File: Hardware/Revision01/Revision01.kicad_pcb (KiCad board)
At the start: 4 copper layers, 100 x 119.8 mm, 84 parts, among them J1 Battery connector, J2 StrainConn, J3 StrainConn, J4 StrainConn, J5 StrainConn, J6 StrainConn, J7 StrainConn, J8 StrainConn, J9 StrainConn, Q1 PMOS, Q2 NMOS, Q3 PMOS, SW1 SW_SPST_LED, U1 NCP1117LPST50T3G, U2 NUCLEO-L476RG, U4 LP5813BDRRR, U5 MRF89XAM9AT-I/RM, U6 ICM-45605

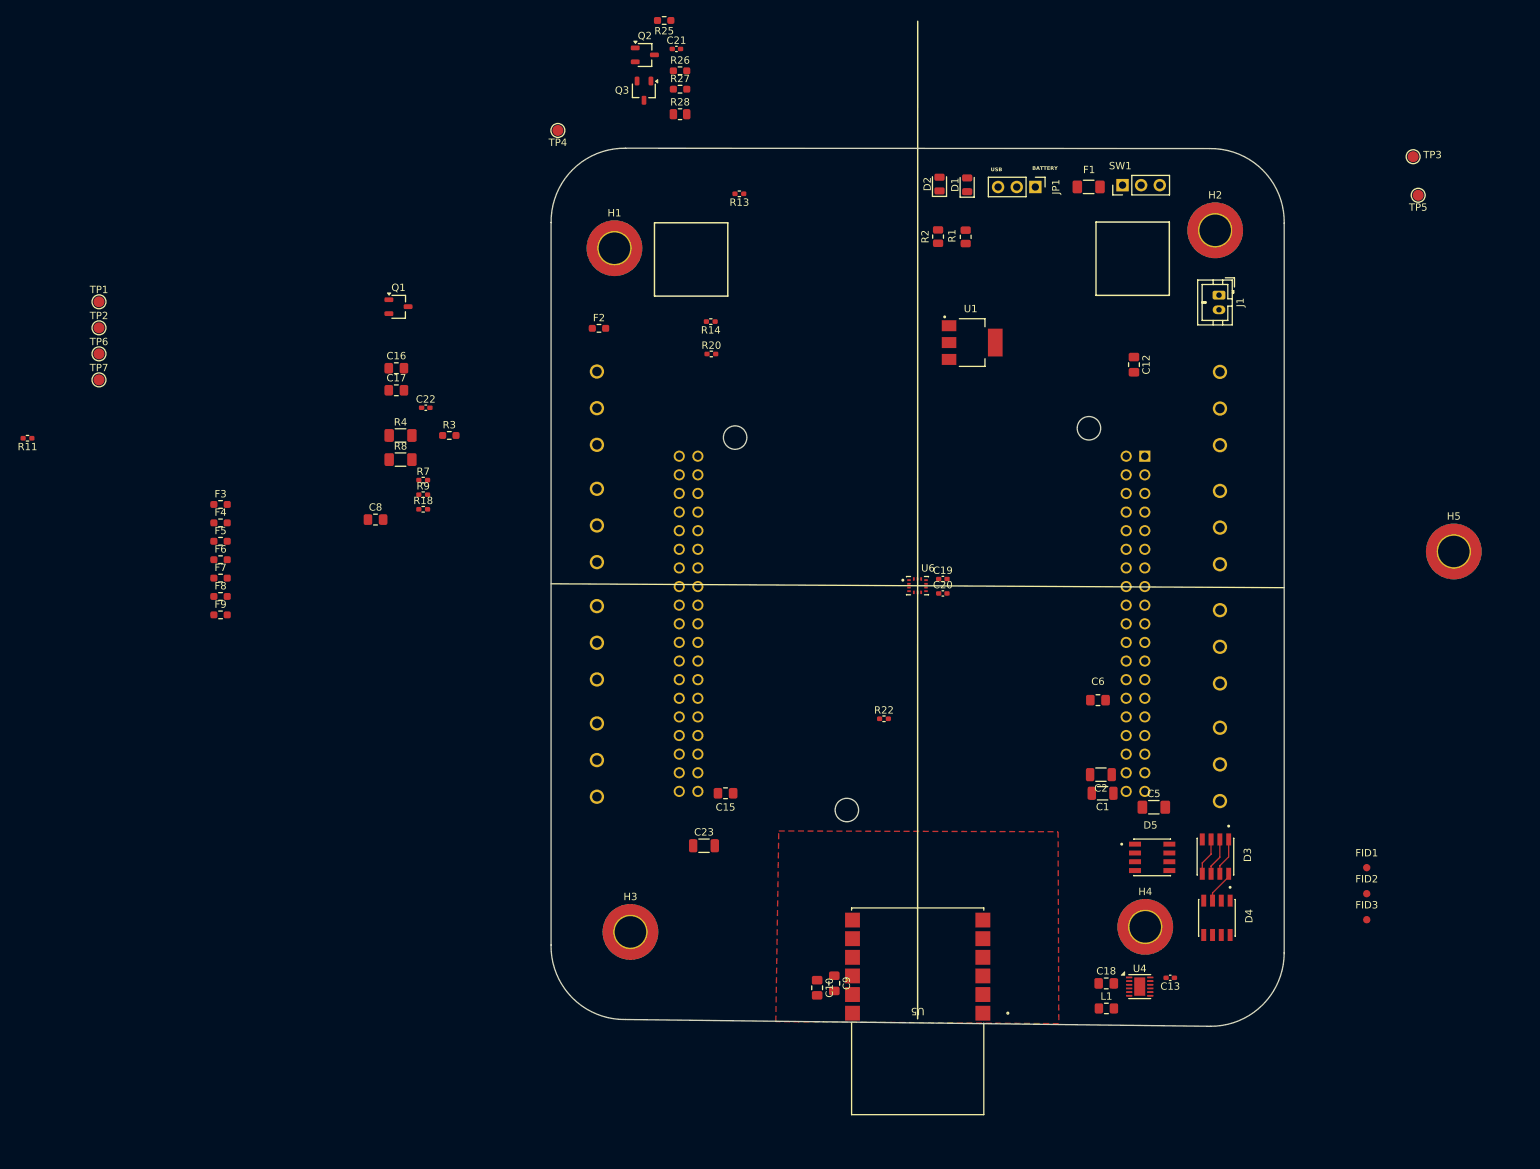
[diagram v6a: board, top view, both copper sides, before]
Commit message: Started working on PART B schematic, making small changes on PART A
ADC uncertainty calculated to be 1.22%
Added External GPIO's that may or may not use
	 start/stop, indication RGB leds

Started working on PART B schematic on ALTIUM, properly imported components with footprints
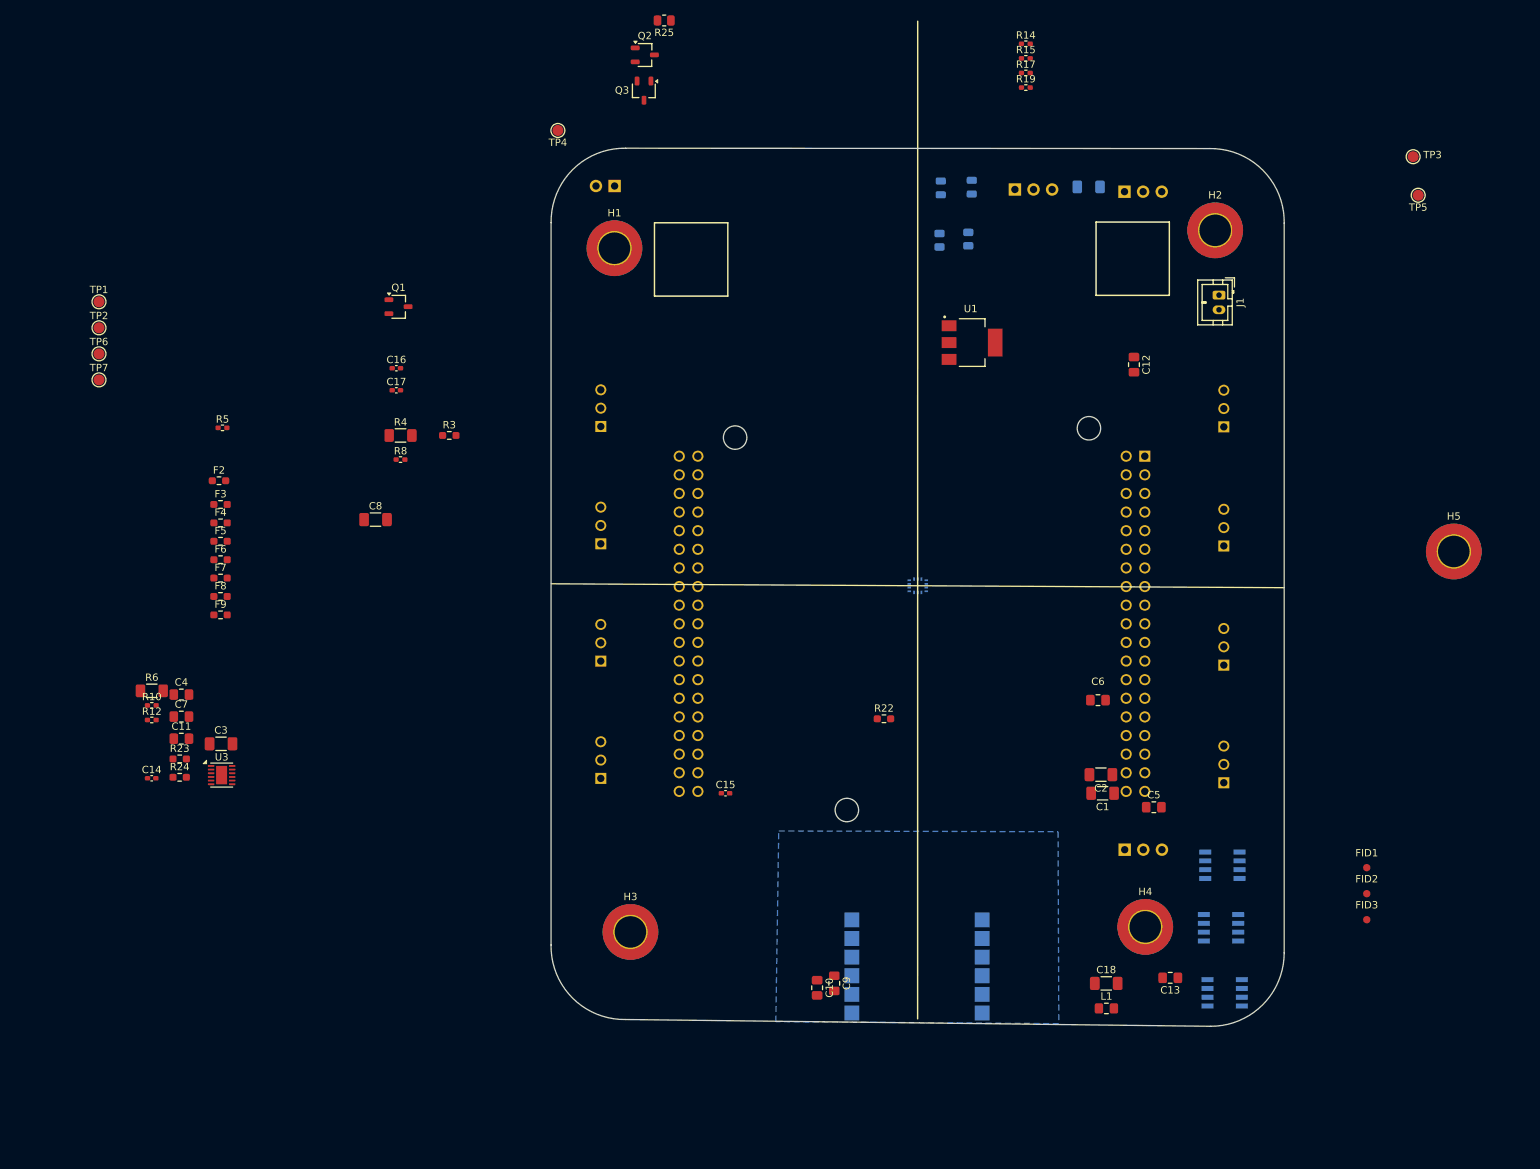
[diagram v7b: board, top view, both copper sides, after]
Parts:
- removed C19, C20, C21, C22: 0.1uF, Capacitor_SMD:C_0402_1005Metric_Pad0.74x0.62mm_HandSolder
- removed C23: 10uF, Capacitor_SMD:C_1206_3216Metric
- removed R11, R13, R18, R20, R7, R9: 1.6K +-1%, Resistor_SMD:R_0402_1005Metric_Pad0.72x0.64mm_HandSolder
- removed R26: 10K +-1%, Resistor_SMD:R_0603_1608Metric_Pad0.98x0.95mm_HandSolder
- removed R27: 15K +-1%, Resistor_SMD:R_0603_1608Metric_Pad0.98x0.95mm_HandSolder
- removed R28: 3.3K +-1%, Resistor_SMD:R_0805_2012Metric
- removed U6: ICM-45605, ICM-45605-gyroscope:XDCR_ICM-45605
- added C11: 10nF, Capacitor_SMD:C_0805_2012Metric_Pad1.18x1.45mm_HandSolder, F.Cu at (60.6, 113.5)
- added C14: 0.1uF, Capacitor_SMD:C_0402_1005Metric_Pad0.74x0.62mm_HandSolder, F.Cu at (56.5, 118.9)
- added C3: 100uF, Capacitor_SMD:C_1206_3216Metric_Pad1.33x1.80mm_HandSolder, F.Cu at (66.0, 114.2)
- added C4: 10nF, Capacitor_SMD:C_0805_2012Metric_Pad1.18x1.45mm_HandSolder, F.Cu at (60.6, 107.5)
- added C7: 10nF, Capacitor_SMD:C_0805_2012Metric_Pad1.18x1.45mm_HandSolder, F.Cu at (60.6, 110.5)
- added D6: RGBW_LED, RGBW:SOL120P540X160-8N, B.Cu at (202.9, 148.2)
- added R10: 1.6K +-1%, Resistor_SMD:R_0402_1005Metric_Pad0.72x0.64mm_HandSolder, F.Cu at (56.6, 109.0)
- added R12: 1.6K +-1%, Resistor_SMD:R_0402_1005Metric_Pad0.72x0.64mm_HandSolder, F.Cu at (56.6, 110.9)
- added R15: 1.6K +-1%, Resistor_SMD:R_0402_1005Metric_Pad0.72x0.64mm_HandSolder, F.Cu at (175.8, 20.7)
- added R17: 1.6K +-1%, Resistor_SMD:R_0402_1005Metric_Pad0.72x0.64mm_HandSolder, F.Cu at (175.8, 22.7)
- added R19: 1.6K +-1%, Resistor_SMD:R_0402_1005Metric_Pad0.72x0.64mm_HandSolder, F.Cu at (175.8, 24.7)
- added R23: 10K +-1%, Resistor_SMD:R_0603_1608Metric_Pad0.98x0.95mm_HandSolder, F.Cu at (60.4, 116.2)
- added R24: 15K +-1%, Resistor_SMD:R_0603_1608Metric_Pad0.98x0.95mm_HandSolder, F.Cu at (60.4, 118.8)
- added R5: 1.6K +-1%, Resistor_SMD:R_0402_1005Metric_Pad0.72x0.64mm_HandSolder, F.Cu at (66.2, 71.1)
- added R6: 0K +-1%, Resistor_SMD:R_1206_3216Metric_Pad1.30x1.75mm_HandSolder, F.Cu at (56.6, 107.0)
- added SW2: ON/OFF_SW_SPST_LED, Connector_PinHeader_2.54mm:PinHeader_1x03_P2.54mm_Vertical, B.Cu at (189.2, 38.9)
- added U3: LP5813BDRRR, Package_SON:WSON-12-1EP_3x3mm_P0.5mm_EP1.5x2.5mm, F.Cu at (66.1, 118.5)
- C1, C2: footprint Capacitor_SMD:C_1206_3216Metric -> Capacitor_SMD:C_1206_3216Metric_Pad1.33x1.80mm_HandSolder
- C13: value 10uF -> 22uF; footprint Capacitor_SMD:C_0402_1005Metric_Pad0.74x0.62mm_HandSolder -> Capacitor_SMD:C_0805_2012Metric_Pad1.18x1.45mm_HandSolder
- C15, C16, C17: value 10nF -> 0.1uF; footprint Capacitor_SMD:C_0805_2012Metric_Pad1.18x1.45mm_HandSolder -> Capacitor_SMD:C_0402_1005Metric_Pad0.74x0.62mm_HandSolder
- C18: value 22uF -> 10uF; footprint Capacitor_SMD:C_0805_2012Metric_Pad1.18x1.45mm_HandSolder -> Capacitor_SMD:C_1206_3216Metric_Pad1.33x1.80mm_HandSolder
- C5: value 100uF -> 10nF; footprint Capacitor_SMD:C_1206_3216Metric_Pad1.33x1.80mm_HandSolder -> Capacitor_SMD:C_0805_2012Metric_Pad1.18x1.45mm_HandSolder
- C8: value 10nF -> 10uF; footprint Capacitor_SMD:C_0805_2012Metric_Pad1.18x1.45mm_HandSolder -> Capacitor_SMD:C_1206_3216Metric_Pad1.33x1.80mm_HandSolder
- D1, D2, D4, D5, F1, JP1, R1, R2: moved to B.Cu
- D3: value RGBW_LED -> Indicication_RGB_Led; footprint RGBW:SOL120P540X160-8N -> Connector_PinHeader_2.54mm:PinHeader_1x03_P2.54mm_Vertical; moved to B.Cu
- J2, J3, J4, J5, J6, J7, J8, J9: footprint 691137710003:691137710003 -> JST:JST_B3B-XH-A
- R22: value 1.6K +-1% -> 10K +-1%; footprint Resistor_SMD:R_0402_1005Metric_Pad0.72x0.64mm_HandSolder -> Resistor_SMD:R_0603_1608Metric_Pad0.98x0.95mm_HandSolder
- R25: value 10K +-1% -> 3.3K +-1%; footprint Resistor_SMD:R_0603_1608Metric_Pad0.98x0.95mm_HandSolder -> Resistor_SMD:R_0805_2012Metric
- R8: value 0K +-1% -> 1.6K +-1%; footprint Resistor_SMD:R_1206_3216Metric_Pad1.30x1.75mm_HandSolder -> Resistor_SMD:R_0402_1005Metric_Pad0.72x0.64mm_HandSolder
- SW1: value SW_SPST_LED -> StartStop_Push; footprint Connector_PinHeader_2.54mm:PinHeader_1x03_P2.54mm_Vertical -> Connector_PinHeader_2.54mm:PinHeader_1x02_P2.54mm_Vertical; moved to B.Cu
- U4: value LP5813BDRRR -> MRF89XAM9AT-I/RM; footprint Package_SON:WSON-12-1EP_3x3mm_P0.5mm_EP1.5x2.5mm -> MRF89XAM9AT-antenna:MOD_MRF89XAM9A_MCH; moved to B.Cu
- U5: value MRF89XAM9AT-I/RM -> ICM-45605; footprint MRF89XAM9AT-antenna:MOD_MRF89XAM9A_MCH -> ICM-45605-gyroscope:XDCR_ICM-45605; moved to B.Cu
- moved SW1 69.3 mm to (119.7, 38.1)
- moved U5 58.0 mm to (161.0, 92.6), turned to 0 degrees
- moved R14 57.3 mm to (175.8, 18.7), turned to 0 degrees
- moved F2 55.8 mm to (65.7, 78.3)
- moved U4 30.6 mm to (160.9, 150.7)
- moved D5 13.4 mm to (202.4, 139.3), turned to 180 degrees
- moved D3 12.4 mm to (189.3, 128.6)
- moved D4 7.21 mm to (202.6, 130.8), turned to 180 degrees
- moved D2 4.42 mm to (168.4, 38.3)
- moved R2 4.13 mm to (167.9, 45.3)
- moved D1 3.62 mm to (164.2, 38.4)
- moved R1 3.60 mm to (164.0, 45.5)
- moved JP1 2.81 mm to (174.3, 38.6)
- turned F1 to 180 degrees
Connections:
- C10 pad 1: /AIN_4 -> /AIN_6
- C12 pad 1: /AIN_5 -> /AIN_8
- C13 pad 1: +3.3V -> Net-(U3-VOUT)
- C15 pad 1: /AIN_6 -> +3.3V
- C16 pad 1: /AIN_7 -> /BatteryV_AIN
- C17 pad 1: /AIN_8 -> +3.3V
- C18 pad 1: Net-(U4-VOUT) -> +3.3V
- C5 pad 1: /Application/+StrainV -> /AIN_2
- C6 pad 1: /AIN_1 -> /AIN_3
- C8 pad 1: /AIN_2 -> +3.3V
- C9 pad 1: /AIN_3 -> /AIN_5
- D4 pad 1: /Application/U1_OUT2 -> /Application/U1_OUT1
- D4 pad 2: /Application/U1_OUT3 -> /Application/U1_OUT2
- D4 pad 3: /Application/U1_OUT0 -> /Application/U1_OUT3
- D4 pad 4: /Application/U1_OUT1 -> /Application/U1_OUT0
- D5 pad 1: /Application/U1_OUT3 -> /Application/U1_OUT2
- D5 pad 2: /Application/U1_OUT0 -> /Application/U1_OUT3
- D5 pad 3: /Application/U1_OUT1 -> /Application/U1_OUT0
- D5 pad 4: /Application/U1_OUT2 -> /Application/U1_OUT1
- F1 pad 2: Net-(SW1-K) -> Net-(SW2-K)
- L1 pad 2: Net-(U4-SW) -> Net-(U3-SW)
- R22 pad 1: /Application/OpAmpOutput8 -> Earth
- R22 pad 2: /AIN_8 -> /BatteryV_Div_Enable_GPIO
- R25 pad 2: /BatteryV_Div_Enable_GPIO -> /BatteryV_AIN
- R8 pad 1: Net-(Q1-S) -> /Application/OpAmpOutput2
- R8 pad 2: +3.3V -> /AIN_2
- SW1 pad 1: Net-(SW1-K) -> /STARTSTOP_GPIO
- SW1 pad 2: Net-(J1-Pin_2) -> Earth
- U2 pad CN10_21: unconnected-(U2B-PA9-PadCN10_21) -> /STARTSTOP_GPIO
- U4 pad 1: Net-(U4-SW) -> Earth
- U4 pad 10: /Application/U1_OUT0 -> +3.3V
- U4 pad 11: /LP5813_EN_GPIO -> Earth
- U4 pad 12: +3.3V -> Earth
- U4 pad 2: Net-(U4-VOUT) -> /ANT_RESET_ANT_GPIO
- U4 pad 3: Earth -> /ANT_CSCON_GPIO
- U4 pad 4: unconnected-(U4-SYNC-Pad4) -> /ANT_IRQ0_GPIO
- U4 pad 5: /I2C_SCL -> /PB15_SPI2_MOSI
- U4 pad 6: /I2C_SDA -> /PB13_SPI2_SCK
- U4 pad 7: /Application/U1_OUT3 -> /PB14_SPI2_MISO
- U4 pad 8: /Application/U1_OUT2 -> /ANT_CSDATA_GPIO
- U4 pad 9: /Application/U1_OUT1 -> /ANT_IRQ1_GPIO
- U5 pad 1: Earth -> /PB14_SPI2_MISO
- U5 pad 10: +3.3V -> unconnected-(U5-RESV_10-Pad10)
- U5 pad 11: Earth -> unconnected-(U5-RESV_11-Pad11)
- U5 pad 12: Earth -> /ICM_CS_GPIO
- U5 pad 2: /ANT_RESET_ANT_GPIO -> unconnected-(U5-RESV/MAS_DA-Pad2)
- U5 pad 3: /ANT_CSCON_GPIO -> unconnected-(U5-RESV/MAS_CLK-Pad3)
- U5 pad 4: /ANT_IRQ0_GPIO -> /ICM_INT1_GPIO
- U5 pad 5: /PB15_SPI2_MOSI -> +3.3V
- U5 pad 6: /PB13_SPI2_SCK -> Earth
- U5 pad 7: /PB14_SPI2_MISO -> unconnected-(U5-RESV_7-Pad7)
- U5 pad 8: /ANT_CSDATA_GPIO -> +3.3V
- U5 pad 9: /ANT_IRQ1_GPIO -> /ICM_INT2_GPIO
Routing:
- net /Application/U1_OUT2: track 5.18 -> 0.00 mm
- net /Application/U1_OUT3: track 5.18 -> 0.00 mm
- net /Application/U1_OUT1: track 5.18 -> 0.00 mm
- net /Application/U1_OUT0: track 4.88 -> 0.00 mm
- added copper zone on B.Cu, net /I2C_SDA
- removed copper zone on F.Cu, net /I2C_SDA
